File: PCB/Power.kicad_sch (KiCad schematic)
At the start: 8 parts, among them Q2 PMOS, U201 LM1117MP-3.3

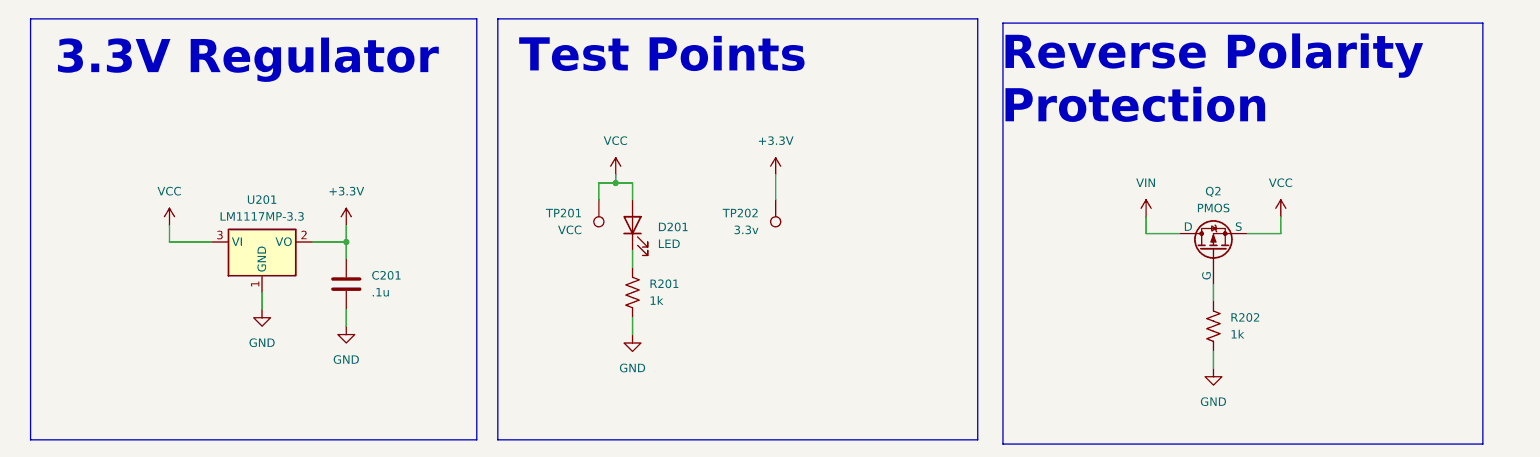
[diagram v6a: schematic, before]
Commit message: - Swapped out 2 LED's for neopixels- Added reverse polarity protection- Replaced Radio module with deticated IC and passives
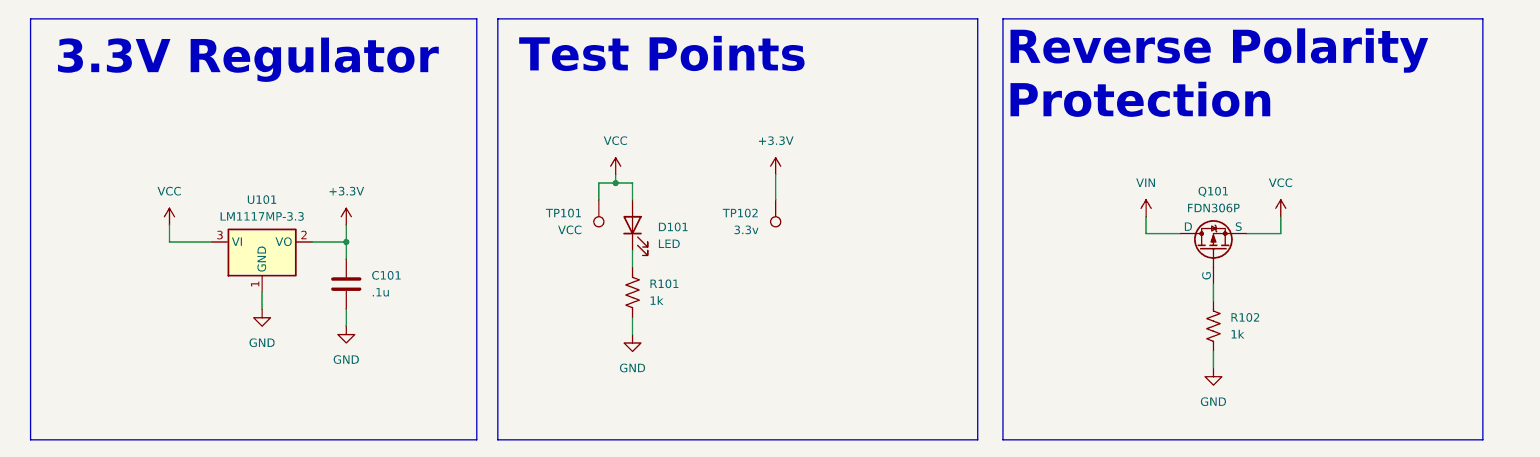
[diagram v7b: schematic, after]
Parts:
- Q101: renamed from Q2; value PMOS -> FDN306P; footprint (none) -> Package_TO_SOT_SMD:SOT-23-3
- renumbered C201 to C101, D201 to D101, R201 to R101, R202 to R102, TP201 to TP101, TP202 to TP102, U201 to U101
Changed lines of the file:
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@@
 	)
 	(rectangle
-		(start 162.56 16.51)
-		(end 234.95 80.01)
+		(start 162.56 15.875)
+		(end 234.95 79.375)
 		(stroke
 			(width 0)
@@
 	(text "Reverse Polarity\nProtection"
 		(exclude_from_sim no)
-		(at 162.306 18.288 0)
+		(at 163.068 17.526 0)
 		(effects
 			(font
@@
 		(dnp no)
 		(fields_autoplaced yes)
-		(property "Reference" "#PWR0209"
+		(property "Reference" "#PWR0108"
 			(at 184.15 49.53 0)
 			(hide yes)
@@
 			(project "Flight Computer"
 				(path "/4254ccd1-49f4-4fe6-9bf7-ccb200d73af4/ce25203d-742b-46bf-b676-aa9cb5879333"
-					(reference "#PWR0209")
+					(reference "#PWR0108")
 					(unit 1)
 				)
@@
 		(dnp no)
 		(fields_autoplaced yes)
-		(property "Reference" "#PWR0203"
+		(property "Reference" "#PWR0101"
 			(at 36.83 50.8 0)
 			(hide yes)
@@
 			(project "Flight Computer"
 				(path "/4254ccd1-49f4-4fe6-9bf7-ccb200d73af4/ce25203d-742b-46bf-b676-aa9cb5879333"
-					(reference "#PWR0203")
+					(reference "#PWR0101")
 					(unit 1)
 				)
@@
 		(dnp no)
 		(fields_autoplaced yes)
-		(property "Reference" "#PWR0205"
+		(property "Reference" "#PWR0102"
 			(at 50.8 66.04 0)
 			(hide yes)
@@
 			(project "Flight Computer"
 				(path "/4254ccd1-49f4-4fe6-9bf7-ccb200d73af4/ce25203d-742b-46bf-b676-aa9cb5879333"
-					(reference "#PWR0205")
+					(reference "#PWR0102")
 					(unit 1)
 				)
@@
 		(dnp no)
 		(fields_autoplaced yes)
-		(property "Reference" "#PWR0206"
+		(property "Reference" "#PWR0104"
 			(at 63.5 68.58 0)
 			(hide yes)
@@
 			(project "Flight Computer"
 				(path "/4254ccd1-49f4-4fe6-9bf7-ccb200d73af4/ce25203d-742b-46bf-b676-aa9cb5879333"
-					(reference "#PWR0206")
+					(reference "#PWR0104")
 					(unit 1)
 				)
@@
 		(dnp no)
 		(fields_autoplaced yes)
-		(property "Reference" "C201"
+		(property "Reference" "C101"
 			(at 67.31 54.6099 0)
 			(show_name no)
@@
 			(project "Flight Computer"
 				(path "/4254ccd1-49f4-4fe6-9bf7-ccb200d73af4/ce25203d-742b-46bf-b676-aa9cb5879333"
-					(reference "C201")
+					(reference "C101")
 					(unit 1)
 				)
@@
 		(dnp no)
 		(fields_autoplaced yes)
-		(property "Reference" "R202"
+		(property "Reference" "R102"
 			(at 196.85 60.9599 0)
 			(show_name no)
@@
 			(project "Flight Computer"
 				(path "/4254ccd1-49f4-4fe6-9bf7-ccb200d73af4/ce25203d-742b-46bf-b676-aa9cb5879333"
-					(reference "R202")
+					(reference "R102")
 					(unit 1)
 				)
@@
 		(dnp no)
 		(fields_autoplaced yes)
-		(property "Reference" "#PWR0204"
+		(property "Reference" "#PWR0103"
 			(at 63.5 50.8 0)
 			(hide yes)
@@
 			(project "Flight Computer"
 				(path "/4254ccd1-49f4-4fe6-9bf7-ccb200d73af4/ce25203d-742b-46bf-b676-aa9cb5879333"
-					(reference "#PWR0204")
+					(reference "#PWR0103")
 					(unit 1)
 				)
@@
 		(dnp no)
 		(fields_autoplaced yes)
-		(property "Reference" "#PWR0202"
+		(property "Reference" "#PWR0107"
 			(at 128.27 43.18 0)
 			(hide yes)
@@
 			(project "Flight Computer"
 				(path "/4254ccd1-49f4-4fe6-9bf7-ccb200d73af4/ce25203d-742b-46bf-b676-aa9cb5879333"
-					(reference "#PWR0202")
+					(reference "#PWR0107")
 					(unit 1)
 				)
@@
 		(dnp no)
 		(fields_autoplaced yes)
-		(property "Reference" "U201"
+		(property "Reference" "U101"
 			(at 50.8 43.18 0)
 			(show_name no)
@@
 			(project "Flight Computer"
 				(path "/4254ccd1-49f4-4fe6-9bf7-ccb200d73af4/ce25203d-742b-46bf-b676-aa9cb5879333"
-					(reference "U201")
+					(reference "U101")
 					(unit 1)
 				)
@@
 		(in_pos_files yes)
 		(dnp no)
-		(property "Reference" "TP201"
+		(property "Reference" "TP101"
 			(at 99.06 45.2119 0)
 			(show_name no)
@@
 			(project "Flight Computer"
 				(path "/4254ccd1-49f4-4fe6-9bf7-ccb200d73af4/ce25203d-742b-46bf-b676-aa9cb5879333"
-					(reference "TP201")
+					(reference "TP101")
 					(unit 1)
 				)
@@
 		(dnp no)
 		(fields_autoplaced yes)
-		(property "Reference" "Q2"
+		(property "Reference" "Q101"
 			(at 194.31 41.91 90)
 			(show_name no)
@@
 			)
 		)
-		(property "Value" "PMOS"
+		(property "Value" "FDN306P"
 			(at 194.31 44.45 90)
 			(show_name no)
@@
 			)
 		)
-		(property "Footprint" ""
+		(property "Footprint" "Package_TO_SOT_SMD:SOT-23-3"
 			(at 191.77 45.72 0)
 			(hide yes)
@@
 			(project "Flight Computer"
 				(path "/4254ccd1-49f4-4fe6-9bf7-ccb200d73af4/ce25203d-742b-46bf-b676-aa9cb5879333"
-					(reference "Q2")
+					(reference "Q101")
 					(unit 1)
 				)
@@
 		(dnp no)
 		(fields_autoplaced yes)
-		(property "Reference" "#PWR0201"
+		(property "Reference" "#PWR0105"
 			(at 104.14 43.18 0)
 			(hide yes)
@@
 			(project "Flight Computer"
 				(path "/4254ccd1-49f4-4fe6-9bf7-ccb200d73af4/ce25203d-742b-46bf-b676-aa9cb5879333"
-					(reference "#PWR0201")
+					(reference "#PWR0105")
 					(unit 1)
 				)
@@
 		(dnp no)
 		(fields_autoplaced yes)
-		(property "Reference" "#PWR0207"
+		(property "Reference" "#PWR0106"
 			(at 106.68 69.85 0)
 			(hide yes)
@@
 			(project "Flight Computer"
 				(path "/4254ccd1-49f4-4fe6-9bf7-ccb200d73af4/ce25203d-742b-46bf-b676-aa9cb5879333"
-					(reference "#PWR0207")
+					(reference "#PWR0106")
 					(unit 1)
 				)
@@
 		(dnp no)
 		(fields_autoplaced yes)
-		(property "Reference" "R201"
+		(property "Reference" "R101"
 			(at 109.22 55.8799 0)
 			(show_name no)
@@
 			(project "Flight Computer"
 				(path "/4254ccd1-49f4-4fe6-9bf7-ccb200d73af4/ce25203d-742b-46bf-b676-aa9cb5879333"
-					(reference "R201")
+					(reference "R101")
 					(unit 1)
 				)
@@
 		(in_pos_files yes)
 		(dnp no)
-		(property "Reference" "TP202"
+		(property "Reference" "TP102"
 			(at 125.73 45.2119 0)
 			(show_name no)
@@
 			(project "Flight Computer"
 				(path "/4254ccd1-49f4-4fe6-9bf7-ccb200d73af4/ce25203d-742b-46bf-b676-aa9cb5879333"
-					(reference "TP202")
+					(reference "TP102")
 					(unit 1)
 				)
@@
 		(dnp no)
 		(fields_autoplaced yes)
-		(property "Reference" "D201"
+		(property "Reference" "D101"
 			(at 110.49 47.3074 90)
 			(show_name no)
@@
 			(project "Flight Computer"
 				(path "/4254ccd1-49f4-4fe6-9bf7-ccb200d73af4/ce25203d-742b-46bf-b676-aa9cb5879333"
-					(reference "D201")
+					(reference "D101")
 					(unit 1)
 				)
@@
 		(dnp no)
 		(fields_autoplaced yes)
-		(property "Reference" "#PWR0208"
+		(property "Reference" "#PWR0110"
 			(at 204.47 49.53 0)
 			(hide yes)
@@
 			(project "Flight Computer"
 				(path "/4254ccd1-49f4-4fe6-9bf7-ccb200d73af4/ce25203d-742b-46bf-b676-aa9cb5879333"
-					(reference "#PWR0208")
+					(reference "#PWR0110")
 					(unit 1)
 				)
@@
 		(dnp no)
 		(fields_autoplaced yes)
-		(property "Reference" "#PWR0210"
+		(property "Reference" "#PWR0109"
 			(at 194.31 74.93 0)
 			(hide yes)
@@
 			(project "Flight Computer"
 				(path "/4254ccd1-49f4-4fe6-9bf7-ccb200d73af4/ce25203d-742b-46bf-b676-aa9cb5879333"
-					(reference "#PWR0210")
+					(reference "#PWR0109")
 					(unit 1)
 				)

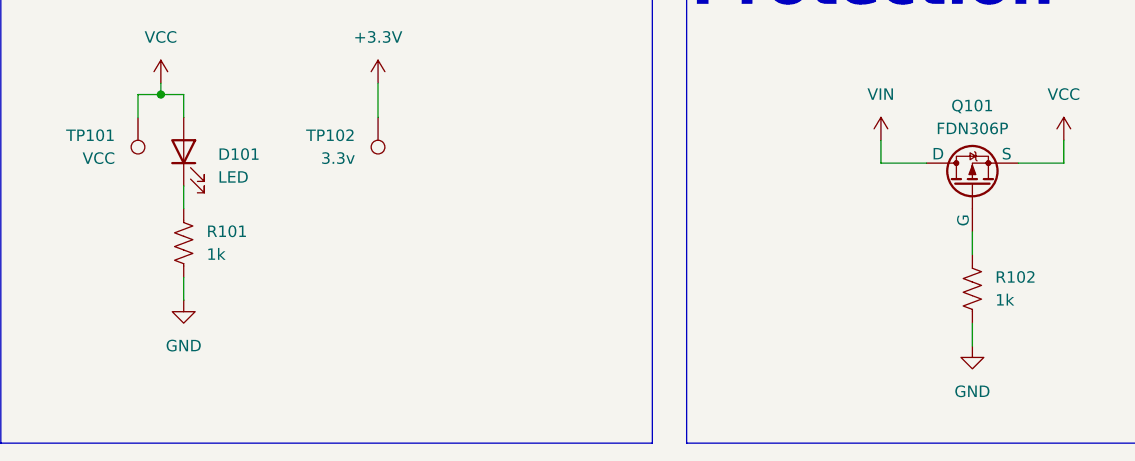
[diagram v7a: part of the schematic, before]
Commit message: - Renamed all NETs connected to MCU sheet to the pin name - Cleaned up schematic - Named all unnamed NETs
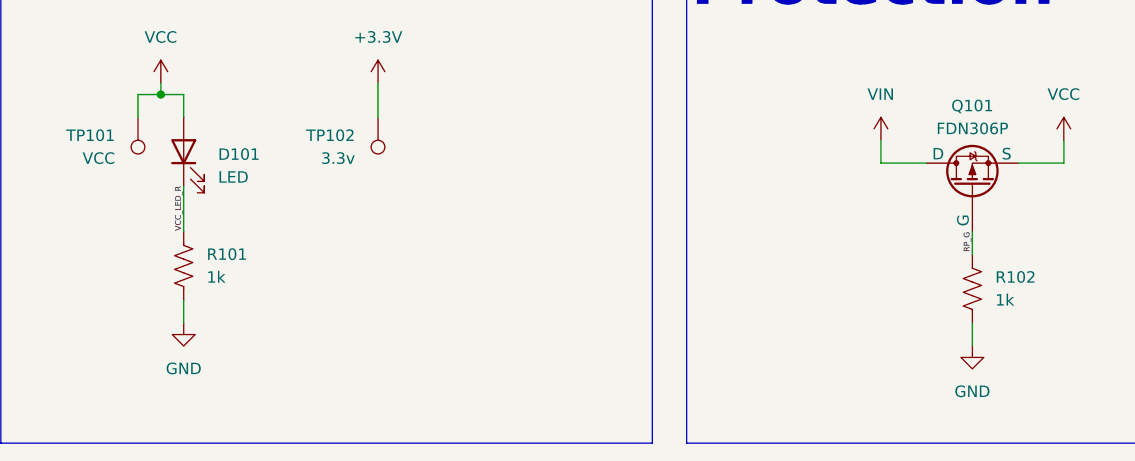
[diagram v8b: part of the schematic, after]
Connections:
- net RP_G: now reaches Q101.2 (G), R102.2
- net VCC_LED_R: now reaches D101.1 (K), R101.2
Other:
- moved on the sheet: R101
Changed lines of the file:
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@@
 	(wire
 		(pts
-			(xy 106.68 50.8) (xy 106.68 53.34)
+			(xy 106.68 50.8) (xy 106.68 55.88)
 		)
 		(stroke
@@
 	(wire
 		(pts
-			(xy 106.68 60.96) (xy 106.68 63.5)
+			(xy 106.68 63.5) (xy 106.68 66.04)
 		)
 		(stroke
 			(width 0)
 			(type default)
+		)
+	)
+	(label "VCC_LED_R"
+		(at 106.68 50.8 270)
+		(effects
+			(font
+				(size 0.635 0.635)
+			)
+			(justify right bottom)
+		)
+	)
+	(label "RP_G"
+		(at 194.31 55.88 270)
+		(effects
+			(font
+				(size 0.635 0.635)
+			)
+			(justify right bottom)
 		)
 	)
@@
 	(symbol
 		(lib_id "power:GND")
-		(at 106.68 63.5 0)
+		(at 106.68 66.04 0)
 		(unit 1)
 		(body_style 1)
@@
 		(fields_autoplaced yes)
 		(property "Reference" "#PWR0106"
-			(at 106.68 69.85 0)
+			(at 106.68 72.39 0)
 			(hide yes)
 			(show_name no)
@@
 		)
 		(property "Value" "GND"
-			(at 106.68 68.58 0)
+			(at 106.68 71.12 0)
 			(show_name no)
 			(do_not_autoplace no)
@@
 		)
 		(property "Footprint" ""
-			(at 106.68 63.5 0)
+			(at 106.68 66.04 0)
 			(hide yes)
 			(show_name no)
@@
 		)
 		(property "Datasheet" ""
-			(at 106.68 63.5 0)
+			(at 106.68 66.04 0)
 			(hide yes)
 			(show_name no)
@@
 		)
 		(property "Description" "Power symbol creates a global label with name \"GND\" , ground"
-			(at 106.68 63.5 0)
+			(at 106.68 66.04 0)
 			(hide yes)
 			(show_name no)
@@
 	(symbol
 		(lib_id "Device:R_US")
-		(at 106.68 57.15 180)
+		(at 106.68 59.69 180)
 		(unit 1)
 		(body_style 1)
@@
 		(fields_autoplaced yes)
 		(property "Reference" "R101"
-			(at 109.22 55.8799 0)
+			(at 109.22 58.4199 0)
 			(show_name no)
 			(do_not_autoplace no)
@@
 		)
 		(property "Value" "1k"
-			(at 109.22 58.4199 0)
+			(at 109.22 60.9599 0)
 			(show_name no)
 			(do_not_autoplace no)
@@
 		)
 		(property "Footprint" "Resistor_SMD:R_0603_1608Metric_Pad0.98x0.95mm_HandSolder"
-			(at 105.664 56.896 90)
+			(at 105.664 59.436 90)
 			(hide yes)
 			(show_name no)
@@
 		)
 		(property "Datasheet" ""
-			(at 106.68 57.15 0)
+			(at 106.68 59.69 0)
 			(hide yes)
 			(show_name no)
@@
 		)
 		(property "Description" "Resistor, US symbol"
-			(at 106.68 57.15 0)
+			(at 106.68 59.69 0)
 			(hide yes)
 			(show_name no)
@@
 		)
 		(property "LCSC" ""
-			(at 106.68 57.15 0)
+			(at 106.68 59.69 0)
 			(hide yes)
 			(show_name no)
@@
 		)
 		(property "LCSC  Part #" ""
-			(at 106.68 57.15 0)
-			(hide yes)
-			(show_name no)
+			(at 106.68 59.69 0)
+			(hide yes)
+			(show_name no)
